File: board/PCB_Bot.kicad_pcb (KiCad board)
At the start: 2 copper layers, 3 parts, among them U1 TB6612FNG, U2 LSM9DS1

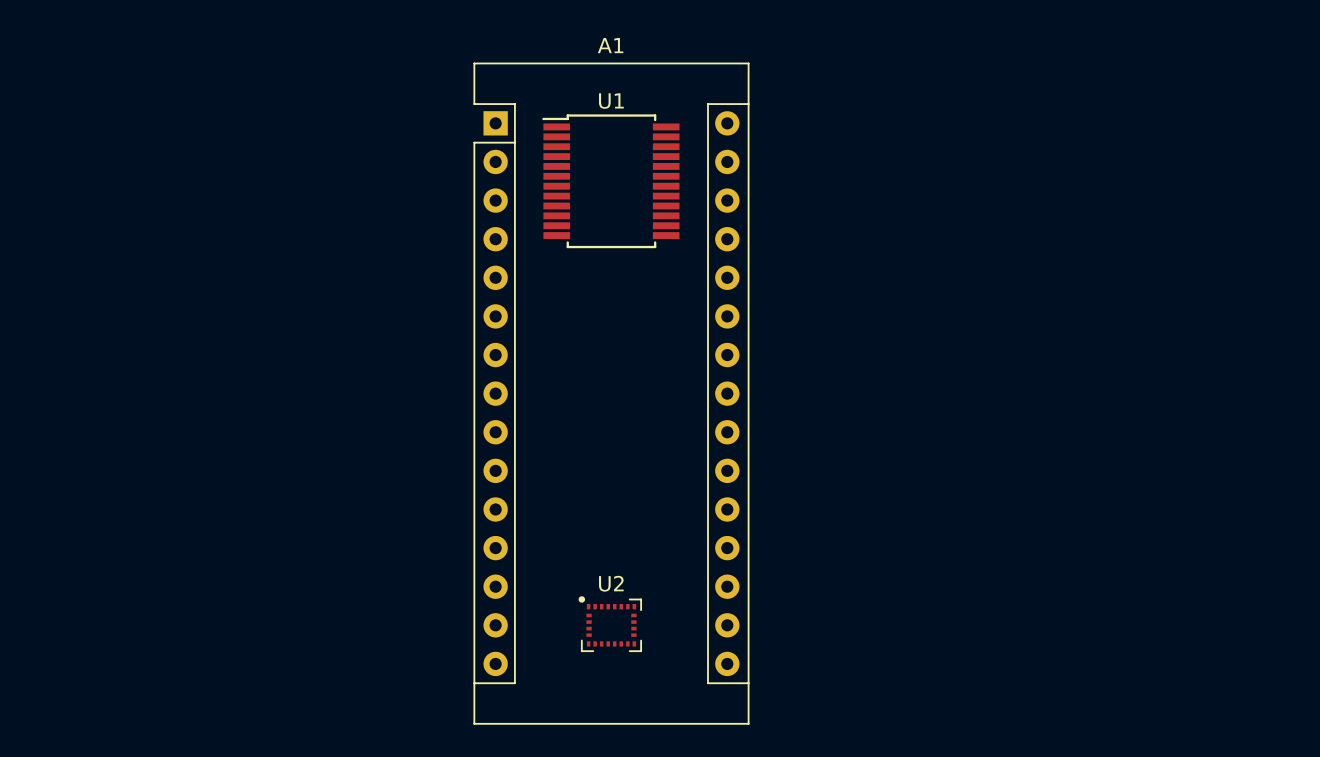
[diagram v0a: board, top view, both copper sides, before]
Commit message: update pcbnew board layout and update foot prints
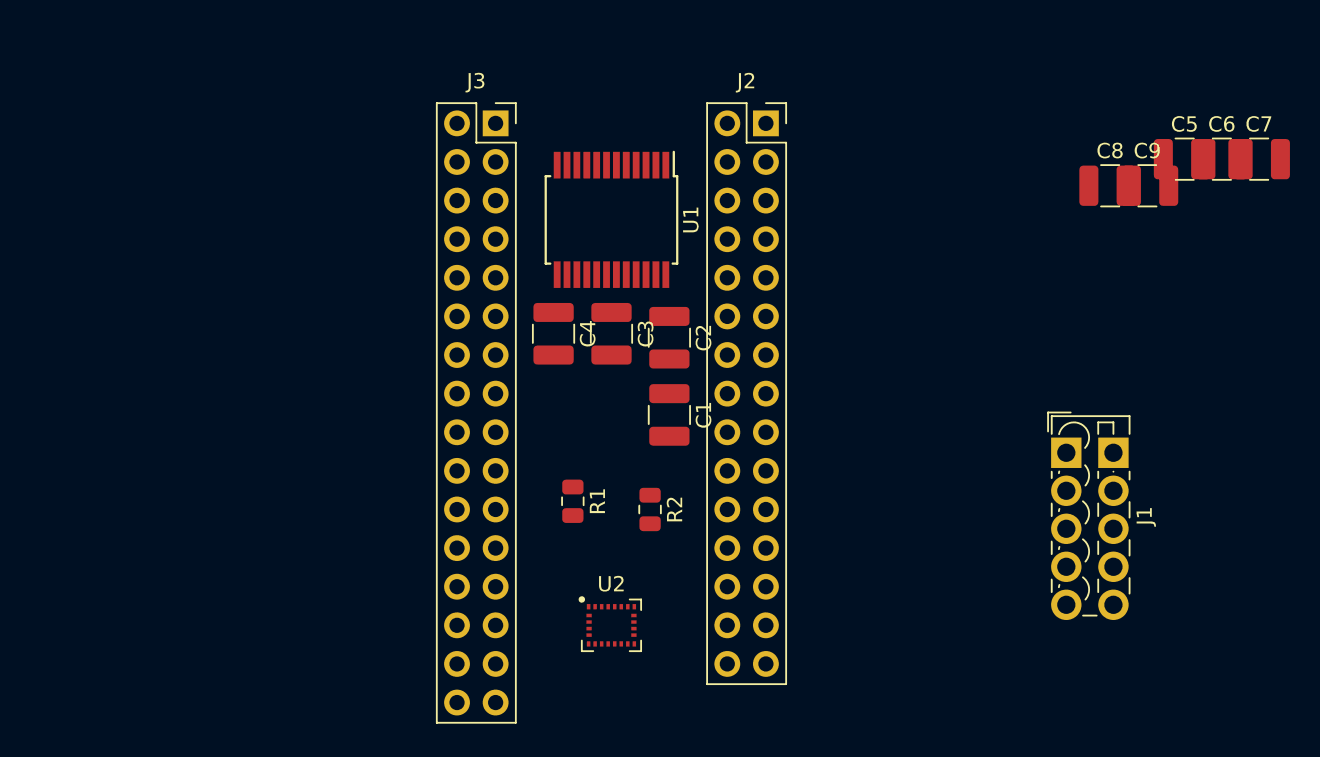
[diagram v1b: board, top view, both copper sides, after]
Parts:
- removed A1: Arduino_Nano_v3.x, Module:Arduino_Nano
- added C1: 0.1uF, Capacitor_SMD:C_1210_3225Metric, F.Cu at (102.9, 91.6)
- added C2: 10uF, Capacitor_SMD:C_1210_3225Metric, F.Cu at (102.9, 86.5)
- added C3: 0.1uF, Capacitor_SMD:C_1210_3225Metric, F.Cu at (99.1, 86.2)
- added C4: 10uF, Capacitor_SMD:C_1210_3225Metric, F.Cu at (95.2, 86.2)
- added C5: 100nF, Capacitor_SMD:C_1210_3225Metric, F.Cu at (136.8, 74.7)
- added C6: 10nF, Capacitor_SMD:C_1210_3225Metric, F.Cu at (139.2, 74.7)
- added C7: 100nF, Capacitor_SMD:C_1210_3225Metric, F.Cu at (141.7, 74.7)
- added C8: 10nF, Capacitor_SMD:C_1210_3225Metric, F.Cu at (131.9, 76.5)
- added C9: 100nF, Capacitor_SMD:C_1210_3225Metric, F.Cu at (134.3, 76.5)
- added J1: Screw_Terminal_01x06, TerminalBlock_Phoenix:TerminalBlock_Phoenix_PTSM-0,5-5-2.5-V-THR_1x05_P2.50mm_Vertical, F.Cu at (129.0, 94.1)
- added J2: Conn_02x15_Top_Bottom, Connector_PinSocket_2.54mm:PinSocket_2x15_P2.54mm_Vertical, F.Cu at (109.2, 72.4)
- added J3: Conn_02x15_Top_Bottom, Connector_PinSocket_2.54mm:PinSocket_2x16_P2.54mm_Vertical, F.Cu at (91.4, 72.4)
- added R1: 4.7K, Resistor_SMD:R_0805_2012Metric, F.Cu at (96.5, 97.2)
- added R2: 4.7K, Resistor_SMD:R_0805_2012Metric, F.Cu at (101.6, 97.8)
- moved U1 2.54 mm to (99.1, 78.7), turned to 270 degrees
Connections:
- U1 pad 1: Net-(U1-Pad1) -> Net-(J1-Pad1)
- U1 pad 10: Net-(U1-Pad10) -> GND
- U1 pad 11: Net-(U1-Pad11) -> Net-(J1-Pad3)
- U1 pad 12: Net-(U1-Pad12) -> Net-(J1-Pad3)
- U1 pad 13: Net-(U1-Pad13) -> VIN
- U1 pad 14: Net-(U1-Pad14) -> VIN
- U1 pad 15: Net-(U1-Pad15) -> D3
- U1 pad 16: Net-(U1-Pad16) -> D4
- U1 pad 17: Net-(U1-Pad17) -> D5
- U1 pad 18: Net-(U1-Pad18) -> GND
- U1 pad 19: Net-(U1-Pad19) -> D6
- U1 pad 2: Net-(U1-Pad2) -> Net-(J1-Pad1)
- U1 pad 20: Net-(U1-Pad20) -> 5V
- U1 pad 21: Net-(U1-Pad21) -> D7
- U1 pad 22: Net-(U1-Pad22) -> D8
- U1 pad 23: Net-(U1-Pad23) -> D9
- U1 pad 24: Net-(U1-Pad24) -> VIN
- U1 pad 3: Net-(U1-Pad3) -> GND
- U1 pad 4: Net-(U1-Pad4) -> GND
- U1 pad 5: Net-(U1-Pad5) -> Net-(J1-Pad2)
- U1 pad 6: Net-(U1-Pad6) -> Net-(J1-Pad2)
- U1 pad 7: Net-(U1-Pad7) -> Net-(J1-Pad4)
- U1 pad 8: Net-(U1-Pad8) -> Net-(J1-Pad4)
- U1 pad 9: Net-(U1-Pad9) -> GND
- U2 pad 1: Net-(U2-Pad1) -> 3V3
- U2 pad 14: Net-(U2-Pad14) -> GND
- U2 pad 15: Net-(U2-Pad15) -> GND
- U2 pad 16: Net-(U2-Pad16) -> GND
- U2 pad 17: Net-(U2-Pad17) -> GND
- U2 pad 18: Net-(U2-Pad18) -> GND
- U2 pad 19: Net-(U2-Pad19) -> GND
- U2 pad 2: Net-(U2-Pad2) -> A5
- U2 pad 20: Net-(U2-Pad20) -> GND
- U2 pad 22: Net-(U2-Pad22) -> 3V3
- U2 pad 23: Net-(U2-Pad23) -> 3V3
- U2 pad 3: Net-(U2-Pad3) -> 3V3
- U2 pad 4: Net-(U2-Pad4) -> A4
- U2 pad 5: Net-(U2-Pad5) -> 3V3
- U2 pad 6: Net-(U2-Pad6) -> 3V3
- U2 pad 7: Net-(U2-Pad7) -> 3V3
- U2 pad 8: Net-(U2-Pad8) -> 3V3

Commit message: Change connectors in schematic and in pcbnew.  add some tracks in pcbnew
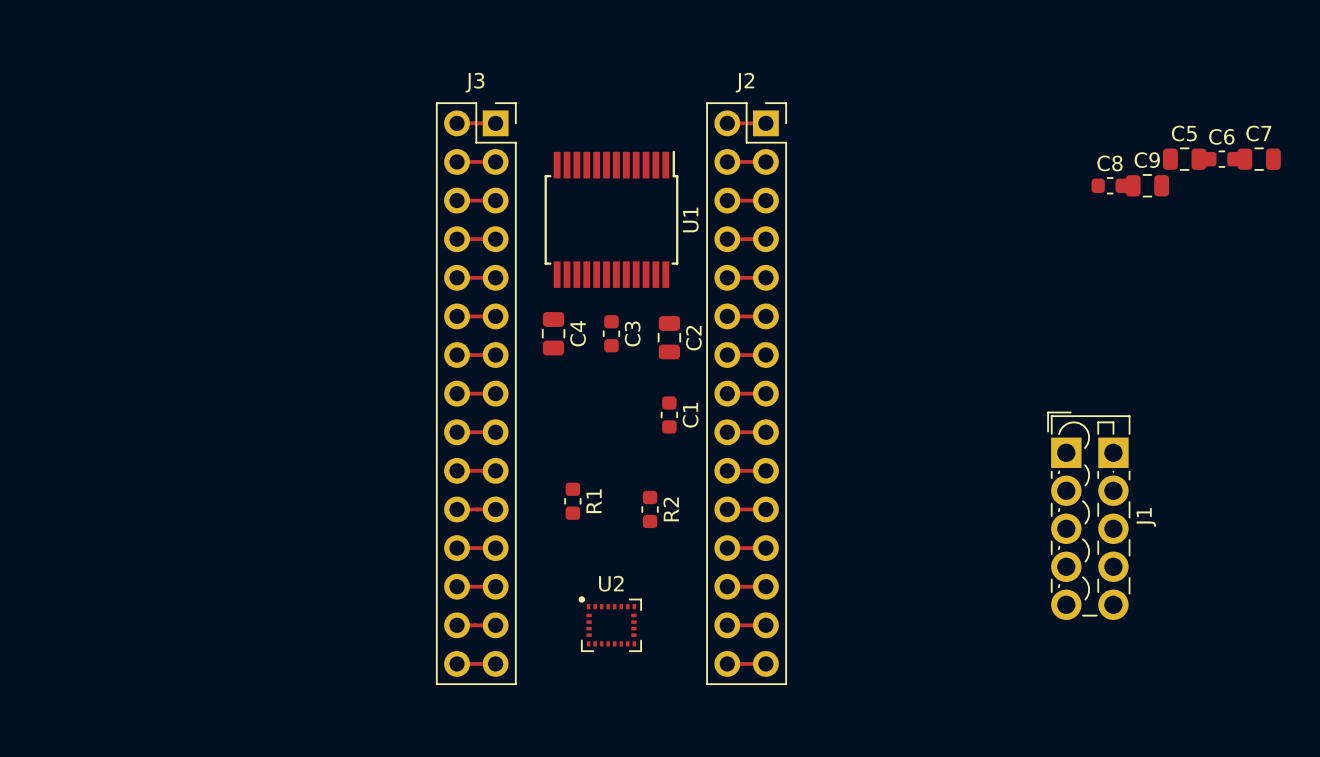
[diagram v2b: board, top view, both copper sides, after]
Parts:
- C1, C3, C6, C8: footprint Capacitor_SMD:C_1210_3225Metric -> Capacitor_SMD:C_0603_1608Metric
- C2, C4, C5, C7, C9: footprint Capacitor_SMD:C_1210_3225Metric -> Capacitor_SMD:C_0805_2012Metric
- J3: footprint Connector_PinSocket_2.54mm:PinSocket_2x16_P2.54mm_Vertical -> Connector_PinSocket_2.54mm:PinSocket_2x15_P2.54mm_Vertical
- R1, R2: footprint Resistor_SMD:R_0805_2012Metric -> Resistor_SMD:R_0603_1608Metric
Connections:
- J2 pad 10: D7 -> D2
- J2 pad 11: D8 -> D3
- J2 pad 12: D9 -> D3
- J2 pad 13: D10 -> D4
- J2 pad 14: D11 -> D4
- J2 pad 15: D12 -> D5
- J2 pad 16: TX1 -> D5
- J2 pad 17: RX0 -> D6
- J2 pad 18: RST -> D6
- J2 pad 19: GND -> D7
- J2 pad 2: RX0 -> TX1
- J2 pad 20: D2 -> D7
- J2 pad 21: D3 -> D8
- J2 pad 22: D4 -> D8
- J2 pad 23: D5 -> D9
- J2 pad 24: D6 -> D9
- J2 pad 25: D7 -> D10
- J2 pad 26: D8 -> D10
- J2 pad 27: D9 -> D11
- J2 pad 28: D10 -> D11
- J2 pad 29: D11 -> D12
- J2 pad 3: RST -> RX0
- J2 pad 4: GND -> RX0
- J2 pad 5: D2 -> RST
- J2 pad 6: D3 -> RST
- J2 pad 7: D4 -> GND
- J2 pad 8: D5 -> GND
- J2 pad 9: D6 -> D2
- J3 pad 10: A2 -> A7
- J3 pad 11: A1 -> A6
- J3 pad 12: A0 -> A6
- J3 pad 13: REF -> A5
- J3 pad 14: 3V3 -> A5
- J3 pad 15: D13 -> A4
- J3 pad 16: VIN -> A4
- J3 pad 17: GND -> A3
- J3 pad 18: RST -> A3
- J3 pad 19: 5V -> A2
- J3 pad 2: GND -> VIN
- J3 pad 20: A7 -> A2
- J3 pad 21: A6 -> A1
- J3 pad 22: A5 -> A1
- J3 pad 23: A4 -> A0
- J3 pad 24: A3 -> A0
- J3 pad 25: A2 -> REF
- J3 pad 26: A1 -> REF
- J3 pad 27: A0 -> 3V3
- J3 pad 28: REF -> 3V3
- J3 pad 29: 3V3 -> D13
- J3 pad 3: RST -> GND
- J3 pad 4: 5V -> GND
- J3 pad 5: A7 -> RST
- J3 pad 6: A6 -> RST
- J3 pad 7: A5 -> 5V
- J3 pad 8: A4 -> 5V
- J3 pad 9: A3 -> A7
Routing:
- net RST: track 0.00 -> 5.08 mm
- net GND: track 0.00 -> 5.08 mm
- net VIN: track 0.00 -> 2.54 mm
- net TX1: track 0.00 -> 2.54 mm
- net RX0: track 0.00 -> 2.54 mm
- net REF: track 0.00 -> 2.54 mm
- net D9: track 0.00 -> 2.54 mm
- net D8: track 0.00 -> 2.54 mm
- net D7: track 0.00 -> 2.54 mm
- net D6: track 0.00 -> 2.54 mm
- net D5: track 0.00 -> 2.54 mm
- net D4: track 0.00 -> 2.54 mm
- net D3: track 0.00 -> 2.54 mm
- net D2: track 0.00 -> 2.54 mm
- net D13: track 0.00 -> 2.54 mm
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
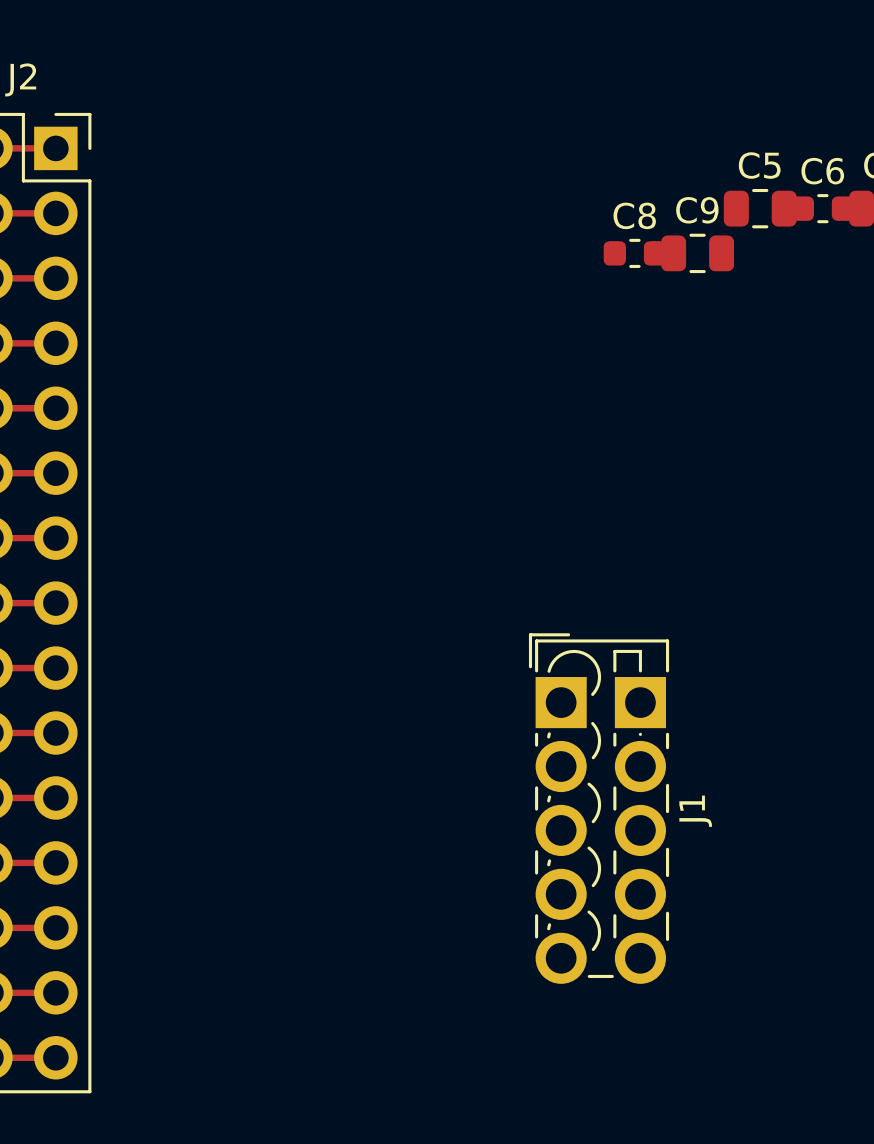
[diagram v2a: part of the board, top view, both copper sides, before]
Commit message: change screw terminals from 1 to 2, add another for RC input
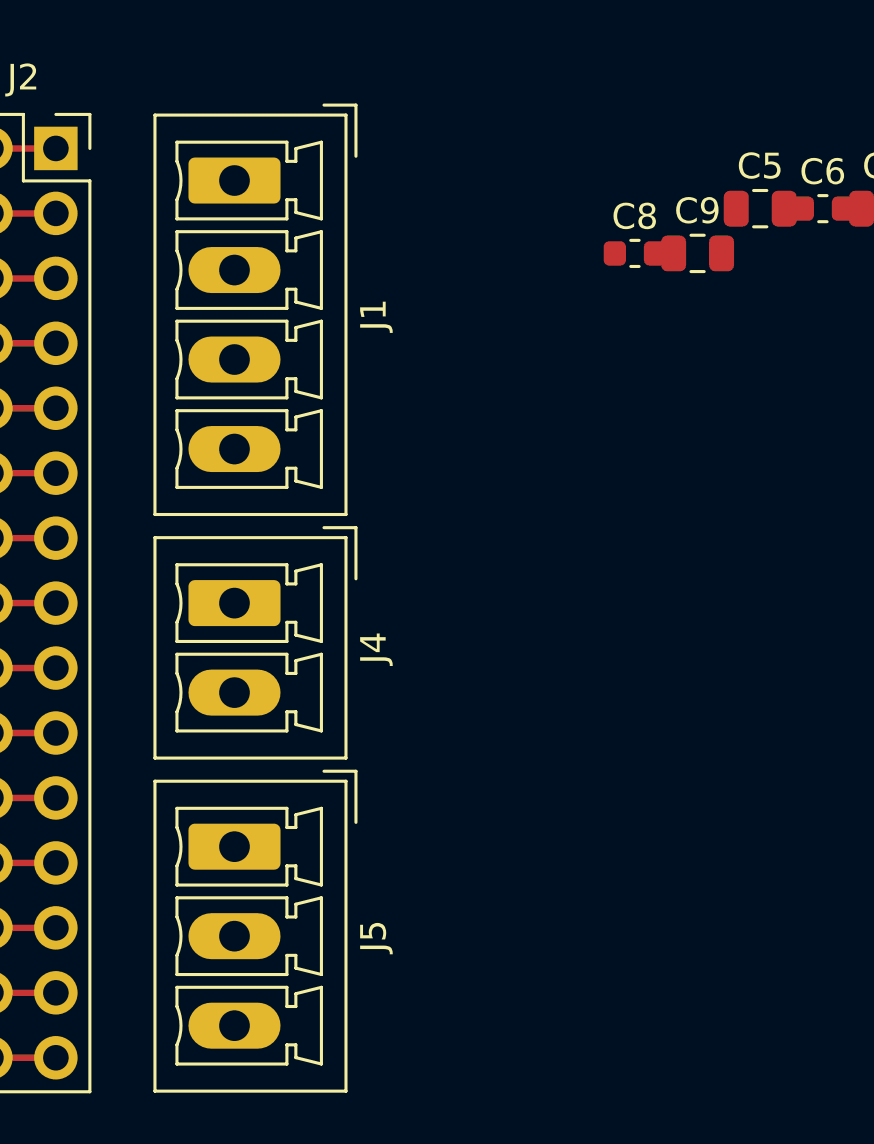
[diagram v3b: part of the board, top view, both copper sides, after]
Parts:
- added J4: Screw_Terminal_01x02, Connector_Phoenix_MC:PhoenixContact_MCV_1,5_2-G-3.5_1x02_P3.50mm_Vertical, F.Cu at (116.2, 90.2)
- added J5: Screw_Terminal_01x03, Connector_Phoenix_MC:PhoenixContact_MCV_1,5_3-G-3.5_1x03_P3.50mm_Vertical, F.Cu at (116.2, 99.7)
- J1: value Screw_Terminal_01x06 -> Screw_Terminal_01x04; footprint TerminalBlock_Phoenix:TerminalBlock_Phoenix_PTSM-0,5-5-2.5-V-THR_1x05_P2.50mm_Vertical -> Connector_Phoenix_MC:PhoenixContact_MCV_1,5_4-G-3.5_1x04_P3.50mm_Vertical
- moved J1 24.1 mm to (116.2, 73.6)

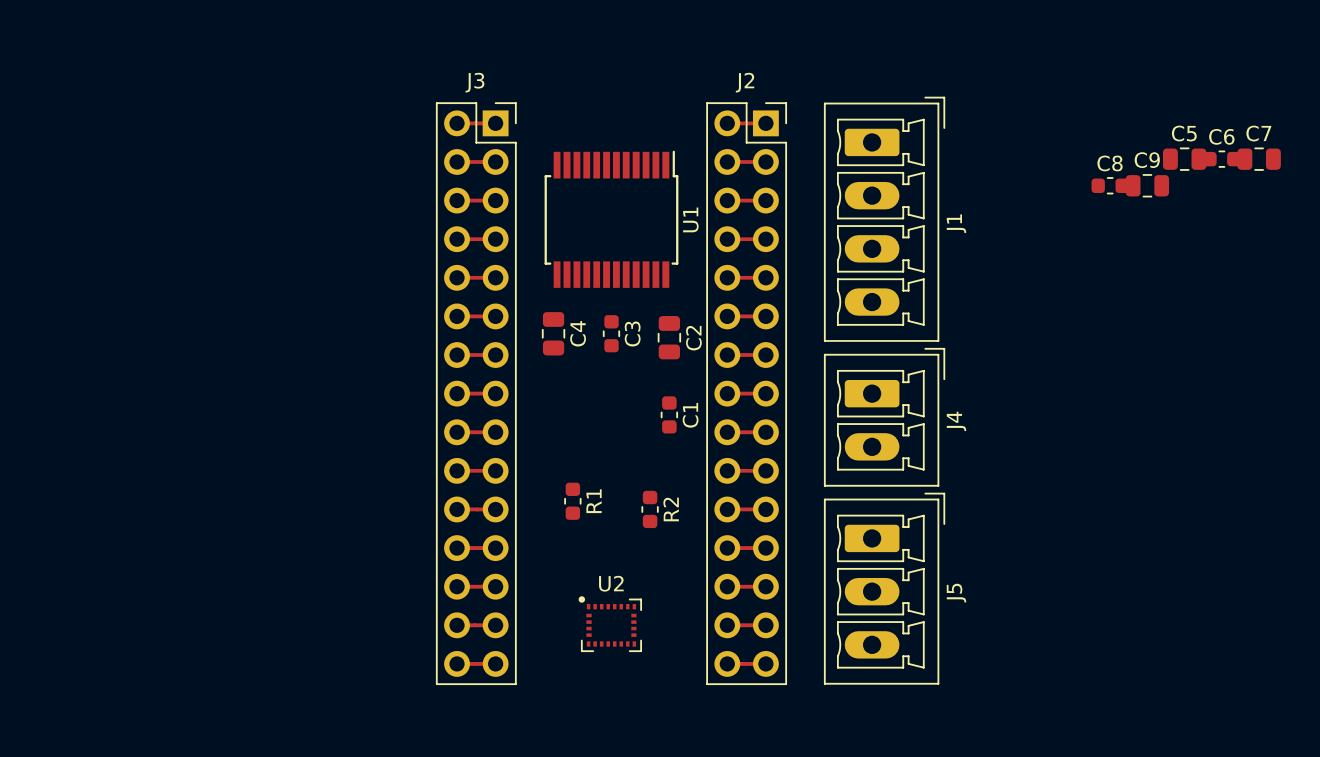
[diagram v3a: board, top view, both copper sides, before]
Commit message: pcbnew move capacitors and resistors around
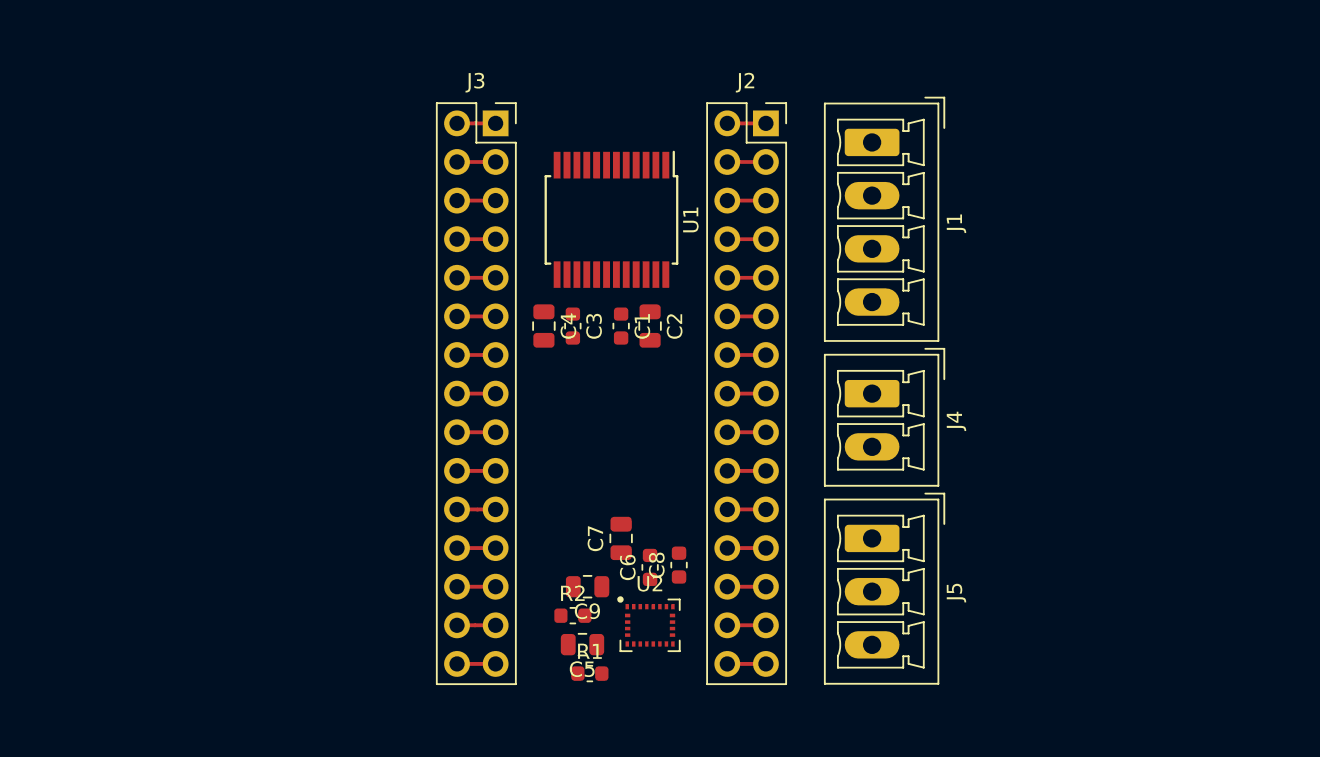
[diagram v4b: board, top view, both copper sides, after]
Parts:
- moved C5 50.9 mm to (97.2, 106.7), turned to 180 degrees
- moved C7 48.8 mm to (99.7, 99.7), turned to 90 degrees
- moved C6 46.2 mm to (101.6, 101.6), turned to 90 degrees
- moved C9 45.3 mm to (97.5, 102.9), turned to 180 degrees
- moved C8 37.8 mm to (103.5, 101.4), turned to 90 degrees
- moved R1 11.4 mm to (97.6, 108.6), turned to 0 degrees
- moved R2 8.64 mm to (96.5, 104.8), turned to 0 degrees
- moved C1 6.65 mm to (99.7, 85.7)
- moved C3 2.59 mm to (96.5, 85.7)
- moved U2 2.54 mm to (101.6, 105.4)
- moved C2 1.48 mm to (101.6, 85.7)
- moved C4 0.81 mm to (94.6, 85.7)
